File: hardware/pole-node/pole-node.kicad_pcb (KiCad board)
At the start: 2 copper layers, 93 x 27.5 mm, 43 parts, among them J1 Anderson, J2 RJ45, J3 Conn_01x03, J4 Conn_01x03, J5 Conn_01x03, J6 Conn_01x03, J7 Anderson, U1 AP3211, U2 MAX485E, U3 MAX485E

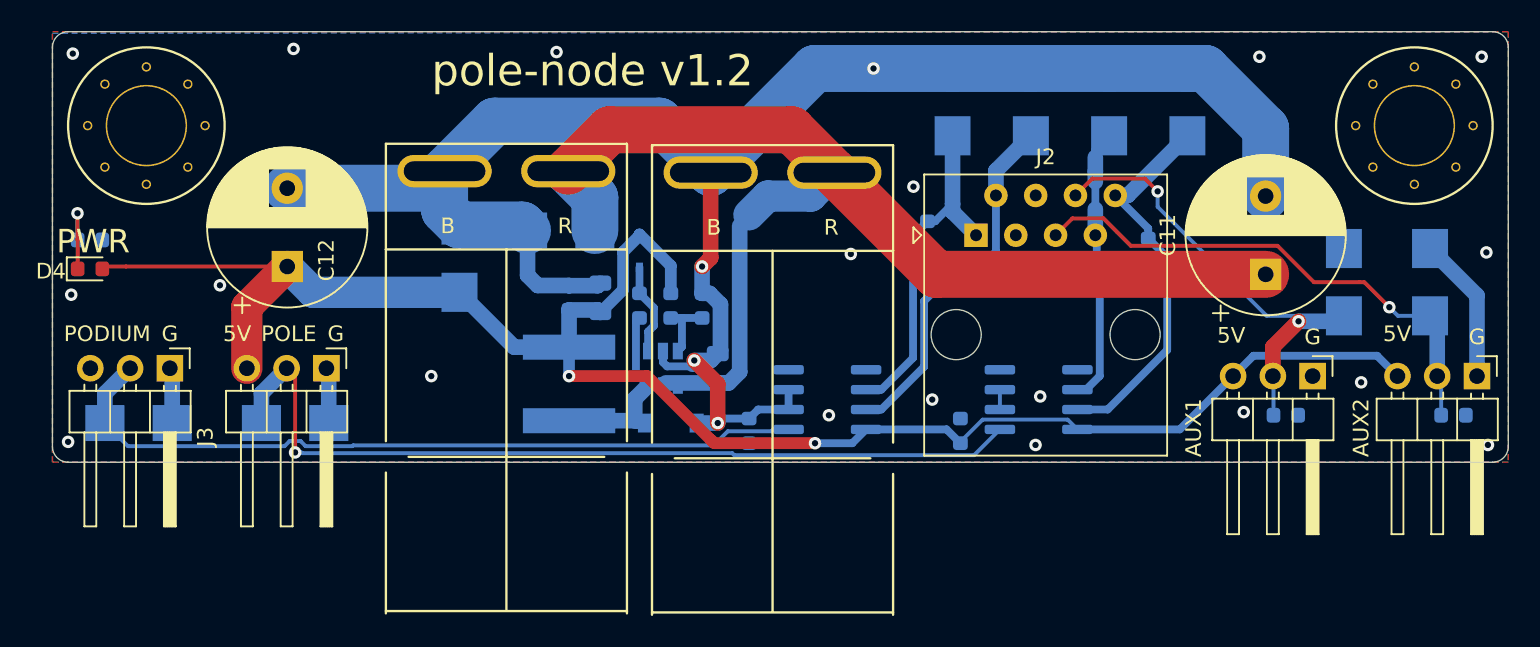
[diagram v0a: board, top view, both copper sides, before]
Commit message: pole-node v1.3:
- Modify to support JLC assembly
  - Change buck converter to one in stock at JLC
- Add protection resistors to IO
- Add PTC fuse and crowbar diode, for reverse voltage protection
- Fix label for grid lights
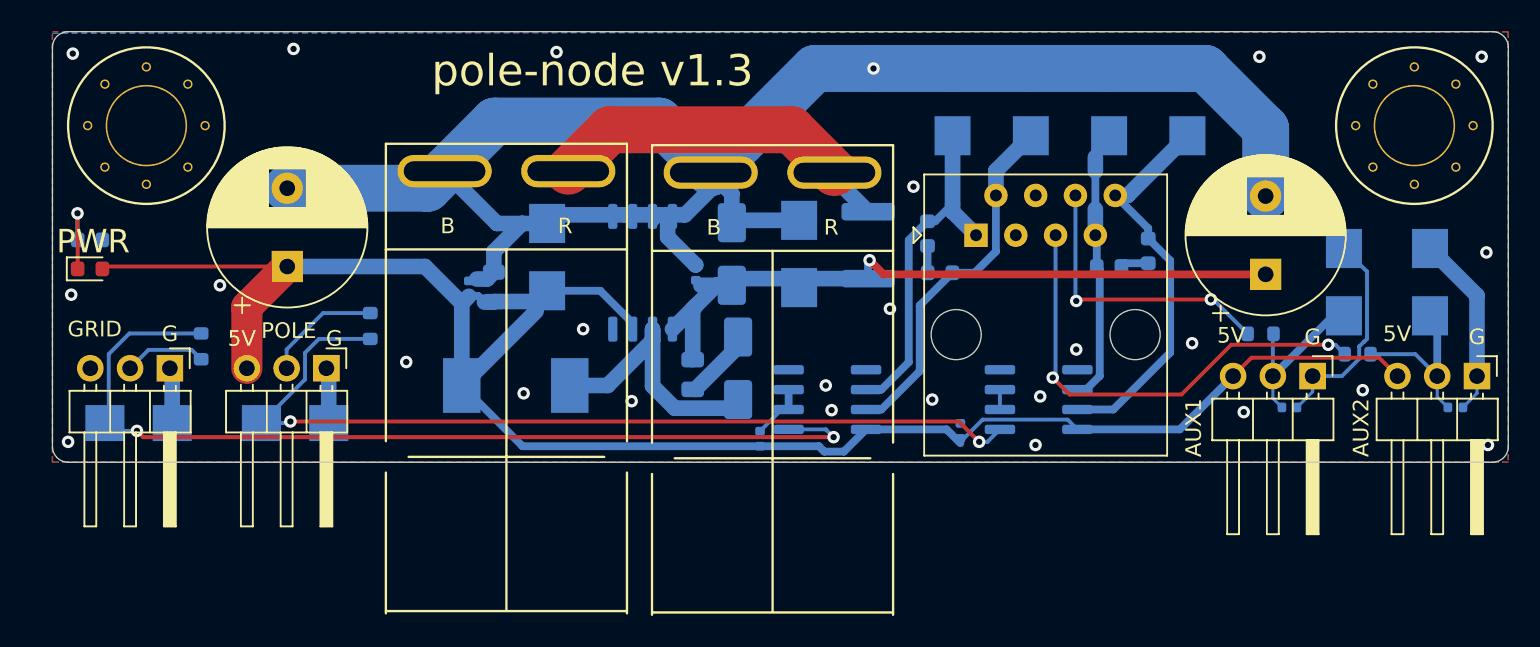
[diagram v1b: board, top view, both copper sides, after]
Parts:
- removed C2: 10nF, Capacitor_SMD:C_0603_1608Metric
- added C13: 100nF, Capacitor_SMD:C_0402_1005Metric, B.Cu at (78.6, 65.4)
- added R6: 470, Resistor_SMD:R_0603_1608Metric, B.Cu at (114.7, 69.3)
- added R7: 470, Resistor_SMD:R_0603_1608Metric, B.Cu at (120.9, 70.6)
- added TH1: PTC 750mA, Fuse:Fuse_1812_4532Metric, B.Cu at (89.6, 63.6)
- C1: value 10uF -> 22uF
- C10, C6, C7, C8, C9: value .1uF -> 100nF; footprint Capacitor_SMD:C_0603_1608Metric -> Capacitor_SMD:C_0402_1005Metric
- D1: footprint Diode_SMD:D_SOD-123 -> Diode_SMD:D_SMA
- D2: value D -> SCHOTTKY; footprint Diode_SMD:D_SOD-323 -> Diode_SMD:D_SMA
- L1: value 5.6uH -> 68uH/2A; footprint Inductor_SMD:L_Taiyo-Yuden_NR-60xx -> Homebrew:L_PROD-Tech_PSPMAA0805
- R1: value 11.5k -> 470
- R2: value 2.21k -> 470
- U1: value AP3211 -> XL1509-5.0E1; footprint Package_TO_SOT_SMD:SOT-23-6 -> Package_SO:SOIC-8_5.23x5.23mm_P1.27mm
- moved R1 30.1 mm to (47.0, 70.1)
- moved R2 21.2 mm to (57.8, 68.8)
- moved D12 15.3 mm to (85.2, 64.2), turned to 90 degrees
- moved C3 6.84 mm to (65.7, 66.3)
- moved C10 6.43 mm to (64.1, 66.4)
- moved U1 6.24 mm to (75.2, 65.4), turned to 90 degrees
- moved D2 5.90 mm to (80.9, 64.2)
- moved D15 5.60 mm to (69.1, 64.4)
- moved D1 5.54 mm to (81.3, 71.5), turned to 90 degrees
- moved L1 3.40 mm to (67.1, 72.6), turned to 180 degrees
- moved C1 1.65 mm to (78.4, 71.9), turned to -90 degrees
- moved C6 0.86 mm to (82.7, 76.0)
- moved C8 0.55 mm to (116.5, 74.0)
- moved C9 0.51 mm to (127.1, 74.0)
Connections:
- C1 pad 1: +12V -> Net-(D12-A1)
- C11 pad 1: +12V -> Net-(D12-A1)
- C8 pad 1: PIR1 -> Net-(D3-A1)
- C9 pad 1: PIR2 -> Net-(D5-A1)
- D1 pad 1: Net-(C2-Pad2) -> Net-(D1-K)
- D12 pad 1: +12V -> Net-(D12-A1)
- D13 pad 1: LED_1_OUT -> Net-(D13-A1)
- D14 pad 1: LED_2_OUT -> Net-(D14-A1)
- D2 pad 1: Net-(C2-Pad1) -> Net-(D12-A1)
- D2 pad 2: +5V -> GND
- D3 pad 1: PIR1 -> Net-(D3-A1)
- D5 pad 1: PIR2 -> Net-(D5-A1)
- J3 pad 3: (no net) -> unconnected-(J3-Pin_3-Pad3)
- J5 pad 2: PIR1 -> Net-(D3-A1)
- J6 pad 2: PIR2 -> Net-(D5-A1)
- L1 pad 1: Net-(C2-Pad2) -> Net-(D1-K)
- R1 pad 1: +5V -> Net-(D13-A1)
- R1 pad 2: Net-(R1-Pad2) -> LED_1_OUT
- R2 pad 1: Net-(R1-Pad2) -> Net-(D14-A1)
- R2 pad 2: GND -> LED_2_OUT
- U1 pad 1: Net-(C2-Pad1) -> Net-(D12-A1)
- U1 pad 2: GND -> Net-(D1-K)
- U1 pad 3: Net-(R1-Pad2) -> +5V
- U1 pad 4: +12V -> GND
- U1 pad 5: +12V -> GND
- U1 pad 6: Net-(C2-Pad2) -> GND
- U2 pad 1: LED_1_OUT -> Net-(D13-A1)
- U2 pad 4: (no net) -> unconnected-(U2-DI-Pad4)
- U3 pad 1: LED_2_OUT -> Net-(D14-A1)
- U3 pad 4: (no net) -> unconnected-(U3-DI-Pad4)
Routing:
- net Net-(D13-A1): track 0.00 -> 59.9 mm, vias 0 -> 2
- net Net-(D14-A1): track 0.00 -> 58.3 mm, vias 0 -> 2
- net +12V: track 74.9 -> 22.3 mm
- net LED_2_OUT: track 55.5 -> 7.50 mm, vias 1 -> 0
- net Net-(D12-A1): track 0.00 -> 46.2 mm, vias 0 -> 1
- net LED_1_OUT: track 49.2 -> 5.28 mm
- net Net-(D1-K): track 0.00 -> 17.1 mm
- net GND: track 139.4 -> 152.3 mm, vias 23 -> 26
- net PIR1: track 31.5 -> 18.7 mm
- net Net-(C2-Pad2): track 12.1 -> 0.00 mm
- net Net-(D5-A1): track 0.00 -> 10.5 mm
- net Net-(D3-A1): track 0.00 -> 10.3 mm
- net Net-(C2-Pad1): track 5.89 -> 0.00 mm
- net Net-(R1-Pad2): track 4.22 -> 0.00 mm
- net PIR2: track 33.6 -> 29.8 mm, vias 1 -> 2
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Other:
- net class Default removed
- board text added: "GRID"
- board text added: "pole-node v1.3"
- board text removed: "PODIUM"
- board text removed: "pole-node v1.2"

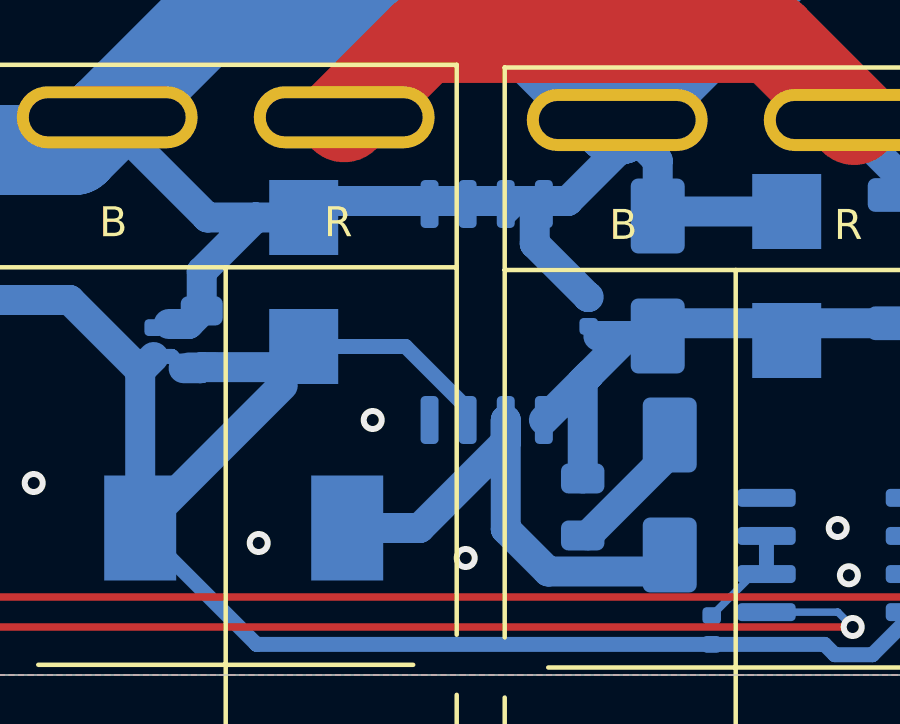
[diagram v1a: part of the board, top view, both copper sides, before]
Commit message: Fix pole-node v1.3 footprint for XL1509 SMPS
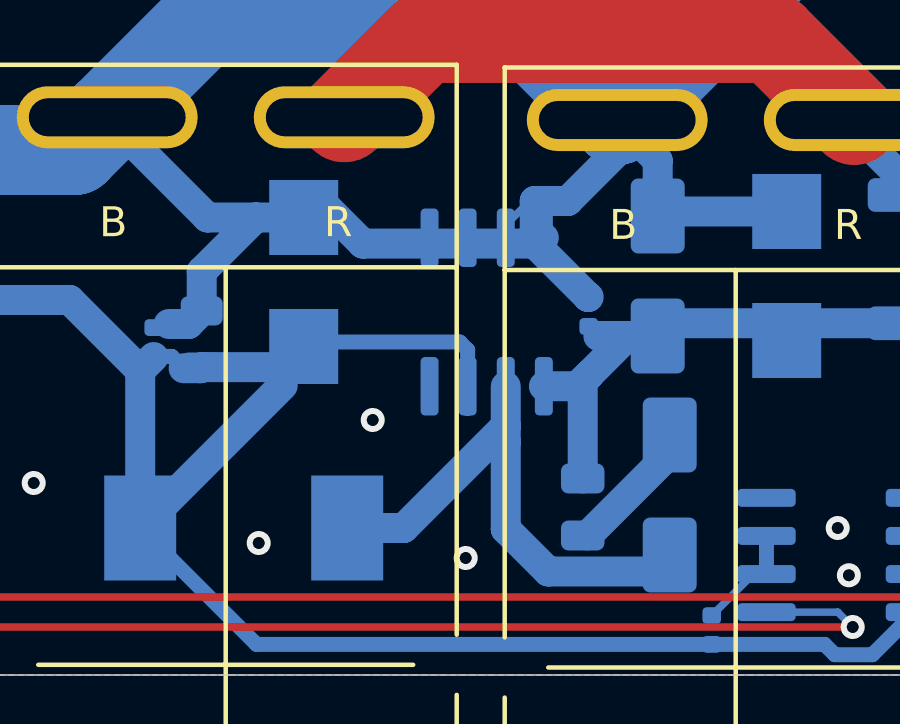
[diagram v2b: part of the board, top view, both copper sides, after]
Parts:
- U1: footprint Package_SO:SOIC-8_5.23x5.23mm_P1.27mm -> Package_SO:SOIC-8_3.9x4.9mm_P1.27mm
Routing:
- net +5V: track 121.5 -> 122.8 mm
- net GND: track 152.3 -> 153.3 mm
- net Net-(D1-K): track 17.1 -> 17.7 mm
